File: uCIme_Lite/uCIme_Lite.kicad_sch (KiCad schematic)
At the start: 0 parts

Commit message: lite: Added power jack power control schematic.
Signed-off-by: Adrien Ricciardi <aricciardi@baylibre.com>
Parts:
- added J? (x2): JACK-C-PC-10A-RA(R), PJ-082BH:JACK-C-PC-10A-RA(R), symbol PJ-082BH:JACK-C-PC-10A-RA(R)
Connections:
- new net GND: J?.2, J?.2, J?.S1 (Shield), J?.S1 (Shield), J?.S2 (Shield), J?.S2 (Shield), J?.S3 (Shield), J?.S3 (Shield), J?.S4 (Shield), J?.S4 (Shield)
- new net Power Management/INPUT_JACK_V+: J?.1
- new net Power Management/OUTPUT_JACK_V+: J?.1
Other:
- added sheet Power Management (Power_Management.kicad_sch)
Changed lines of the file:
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@@
 (kicad_sch (version 20211123) (generator eeschema)
-  (paper "A4")
+  (paper "A3")
   (title_block
     (title "uCIme Lite main page")
@@
     (company "(C) BayLibre")
   )
+  (junction (at 132.08 57.15) (diameter 0) (color 0 0 0 0)
+  )
+  (junction (at 281.94 57.15) (diameter 0) (color 0 0 0 0)
+  )
+  (wire (pts (xy 281.94 50.8) (xy 283.21 50.8))
+    (stroke (width 0) (type default) (color 0 0 0 0))
+  )
+  (wire (pts (xy 130.81 45.72) (xy 177.8 45.72))
+    (stroke (width 0) (type default) (color 0 0 0 0))
+  )
+  (wire (pts (xy 123.19 57.15) (xy 132.08 57.15))
+    (stroke (width 0) (type default) (color 0 0 0 0))
+  )
+  (wire (pts (xy 236.22 45.72) (xy 283.21 45.72))
+    (stroke (width 0) (type default) (color 0 0 0 0))
+  )
+  (wire (pts (xy 130.81 50.8) (xy 132.08 50.8))
+    (stroke (width 0) (type default) (color 0 0 0 0))
+  )
+  (wire (pts (xy 132.08 50.8) (xy 132.08 57.15))
+    (stroke (width 0) (type default) (color 0 0 0 0))
+  )
+  (wire (pts (xy 290.83 55.88) (xy 290.83 57.15))
+    (stroke (width 0) (type default) (color 0 0 0 0))
+  )
+  (wire (pts (xy 281.94 57.15) (xy 290.83 57.15))
+    (stroke (width 0) (type default) (color 0 0 0 0))
+  )
+  (wire (pts (xy 281.94 50.8) (xy 281.94 57.15))
+    (stroke (width 0) (type default) (color 0 0 0 0))
+  )
+  (wire (pts (xy 132.08 57.15) (xy 132.08 58.42))
+    (stroke (width 0) (type default) (color 0 0 0 0))
+  )
+  (wire (pts (xy 281.94 57.15) (xy 281.94 58.42))
+    (stroke (width 0) (type default) (color 0 0 0 0))
+  )
+  (wire (pts (xy 123.19 55.88) (xy 123.19 57.15))
+    (stroke (width 0) (type default) (color 0 0 0 0))
+  )
+  (symbol (lib_id "PJ-082BH:JACK-C-PC-10A-RA(R)") (at 290.83 48.26 0) (mirror y) (unit 1)
+    (in_bom yes) (on_board yes) (fields_autoplaced)
+    (property "Reference" "J?" (id 0) (at 297.18 47.3455 0)
+      (effects (font (size 1.27 1.27)) (justify right))
+    )
+    (property "Value" "JACK-C-PC-10A-RA(R)" (id 1) (at 297.18 49.8855 0)
+      (effects (font (size 1.27 1.27)) (justify right))
+    )
+    (property "Footprint" "PJ-082BH:JACK-C-PC-10A-RA(R)" (id 2) (at 290.83 48.26 0)
+      (effects (font (size 1.27 1.27)) hide)
+    )
+    (property "Datasheet" "" (id 3) (at 290.83 48.26 0)
+      (effects (font (size 1.27 1.27)) hide)
+    )
+    (pin "1")
+    (pin "2")
+    (pin "S1")
+    (pin "S2")
+    (pin "S3")
+    (pin "S4")
+  )
+  (symbol (lib_id "PJ-082BH:JACK-C-PC-10A-RA(R)") (at 123.19 48.26 0) (unit 1)
+    (in_bom yes) (on_board yes) (fields_autoplaced)
+    (property "Reference" "J?" (id 0) (at 123.19 39.37 0))
+    (property "Value" "JACK-C-PC-10A-RA(R)" (id 1) (at 123.19 41.91 0))
+    (property "Footprint" "PJ-082BH:JACK-C-PC-10A-RA(R)" (id 2) (at 123.19 48.26 0)
+      (effects (font (size 1.27 1.27)) hide)
+    )
+    (property "Datasheet" "" (id 3) (at 123.19 48.26 0)
+      (effects (font (size 1.27 1.27)) hide)
+    )
+    (pin "1")
+    (pin "2")
+    (pin "S1")
+    (pin "S2")
+    (pin "S3")
+    (pin "S4")
+  )
+  (symbol (lib_id "power:GND") (at 281.94 58.42 0) (unit 1)
+    (in_bom yes) (on_board yes) (fields_autoplaced)
+    (property "Reference" "#PWR?" (id 0) (at 281.94 64.77 0)
+      (effects (font (size 1.27 1.27)) hide)
+    )
+    (property "Value" "GND" (id 1) (at 281.94 63.5 0))
+    (property "Footprint" "" (id 2) (at 281.94 58.42 0)
+      (effects (font (size 1.27 1.27)) hide)
+    )
+    (property "Datasheet" "" (id 3) (at 281.94 58.42 0)
+      (effects (font (size 1.27 1.27)) hide)
+    )
+    (pin "1")
+  )
+  (symbol (lib_id "power:GND") (at 132.08 58.42 0) (unit 1)
+    (in_bom yes) (on_board yes) (fields_autoplaced)
+    (property "Reference" "#PWR?" (id 0) (at 132.08 64.77 0)
+      (effects (font (size 1.27 1.27)) hide)
+    )
+    (property "Value" "GND" (id 1) (at 132.08 63.5 0))
+    (property "Footprint" "" (id 2) (at 132.08 58.42 0)
+      (effects (font (size 1.27 1.27)) hide)
+    )
+    (property "Datasheet" "" (id 3) (at 132.08 58.42 0)
+      (effects (font (size 1.27 1.27)) hide)
+    )
+    (pin "1")
+  )
+  (sheet (at 177.8 39.37) (size 58.42 31.75) (fields_autoplaced)
+    (stroke (width 0.1524) (type solid) (color 0 0 0 0))
+    (fill (color 0 0 0 0.0000))
+    (property "Sheet name" "Power Management" (id 0) (at 177.8 38.6584 0)
+      (effects (font (size 1.27 1.27)) (justify left bottom))
+    )
+    (property "Sheet file" "Power_Management.kicad_sch" (id 1) (at 177.8 71.7046 0)
+      (effects (font (size 1.27 1.27)) (justify left top))
+    )
+    (pin "INPUT_JACK_V+" input (at 177.8 45.72 180)
+      (effects (font (size 1.27 1.27)) (justify left))
+    )
+    (pin "OUTPUT_JACK_V+" output (at 236.22 45.72 0)
+      (effects (font (size 1.27 1.27)) (justify right))
+    )
+    (pin "JACK_ENABLE" input (at 220.98 71.12 270)
+      (effects (font (size 1.27 1.27)) (justify left))
+    )
+  )
   (sheet_instances
     (path "/" (page "1"))
+    (path "/b72074d7-db6e-4ce2-896d-216adccf1d19" (page "2"))
+  )
+  (symbol_instances
+    (path "/b72074d7-db6e-4ce2-896d-216adccf1d19/02fafa4a-7b73-4e81-8da5-132c6b5c9bff"
+      (reference "#PWR?") (unit 1) (value "GND") (footprint "")
+    )
+    (path "/b72074d7-db6e-4ce2-896d-216adccf1d19/35a86e98-46cc-46df-ad53-81efd104ac95"
+      (reference "#PWR?") (unit 1) (value "GND") (footprint "")
+    )
+    (path "/b72074d7-db6e-4ce2-896d-216adccf1d19/635934cd-3f03-40e6-aa6f-441bbb697ee2"
+      (reference "#PWR?") (unit 1) (value "GND") (footprint "")
+    )
+    (path "/b72074d7-db6e-4ce2-896d-216adccf1d19/7c913419-8c7e-474a-a151-4292df2a9063"
+      (reference "#PWR?") (unit 1) (value "GND") (footprint "")
+    )
+    (path "/b72074d7-db6e-4ce2-896d-216adccf1d19/82d1e808-369e-4a11-819a-83d565227eb4"
+      (reference "#PWR?") (unit 1) (value "GND") (footprint "")
+    )
+    (path "/b72074d7-db6e-4ce2-896d-216adccf1d19/98f27e05-bd7c-4098-9b75-20ce5d30fae5"
+      (reference "#PWR?") (unit 1) (value "GND") (footprint "")
+    )
+    (path "/aaee36d0-4dcf-457a-8eaa-8cb8fea45041"
+      (reference "#PWR?") (unit 1) (value "GND") (footprint "")
+    )
+    (path "/de94efd2-e5d2-4545-9075-dd7613e5777f"
+      (reference "#PWR?") (unit 1) (value "GND") (footprint "")
+    )
+    (path "/b72074d7-db6e-4ce2-896d-216adccf1d19/e31b32d0-c0c6-443a-8ef3-a94aeee3b208"
+      (reference "#PWR?") (unit 1) (value "GND") (footprint "")
+    )
+    (path "/b72074d7-db6e-4ce2-896d-216adccf1d19/17bc7eea-81f3-448e-95b1-8b446b2817f2"
+      (reference "C?") (unit 1) (value "220n") (footprint "Capacitor_SMD:C_0805_2012Metric")
+    )
+    (path "/b72074d7-db6e-4ce2-896d-216adccf1d19/465ff876-8b5f-4366-b4a3-31a49fbb8eed"
+      (reference "C?") (unit 1) (value "220n") (footprint "Capacitor_SMD:C_0805_2012Metric")
+    )
+    (path "/b72074d7-db6e-4ce2-896d-216adccf1d19/630f389e-df29-4fb4-a243-3d74878f7967"
+      (reference "C?") (unit 1) (value "100n") (footprint "Capacitor_SMD:C_0805_2012Metric")
+    )
+    (path "/b72074d7-db6e-4ce2-896d-216adccf1d19/a145c277-00e6-476a-b587-453aa354ab19"
+      (reference "C?") (unit 1) (value "100n") (footprint "Capacitor_SMD:C_0805_2012Metric")
+    )
+    (path "/03e02d60-ba51-4f77-a312-8d67a4adcc67"
+      (reference "J?") (unit 1) (value "JACK-C-PC-10A-RA(R)") (footprint "PJ-082BH:JACK-C-PC-10A-RA(R)")
+    )
+    (path "/3071b057-73f1-47ad-9445-a53f1a251bbe"
+      (reference "J?") (unit 1) (value "JACK-C-PC-10A-RA(R)") (footprint "PJ-082BH:JACK-C-PC-10A-RA(R)")
+    )
+    (path "/b72074d7-db6e-4ce2-896d-216adccf1d19/24df8571-9618-4f38-9191-19c2d92e80ea"
+      (reference "Q?") (unit 1) (value "BUK7M27-80EX") (footprint "Package_TO_SOT_SMD:LFPAK33")
+    )
+    (path "/b72074d7-db6e-4ce2-896d-216adccf1d19/bae3b56c-6075-495b-ac2a-b15d5aaa6fb6"
+      (reference "Q?") (unit 1) (value "BUK7M27-80EX") (footprint "Package_TO_SOT_SMD:LFPAK33")
+    )
+    (path "/b72074d7-db6e-4ce2-896d-216adccf1d19/21cf5ff6-9362-4b6b-a0e8-4d769b623a57"
+      (reference "R?") (unit 1) (value "2.4K") (footprint "Resistor_SMD:R_0805_2012Metric")
+    )
+    (path "/b72074d7-db6e-4ce2-896d-216adccf1d19/8e4f213e-c272-4cc1-a885-011733cd1c99"
+      (reference "R?") (unit 1) (value "10K") (footprint "Resistor_SMD:R_0603_1608Metric")
+    )
+    (path "/b72074d7-db6e-4ce2-896d-216adccf1d19/b2b14a25-12a4-4a13-acce-e2b1fa675d65"
+      (reference "R?") (unit 1) (value "2.4K") (footprint "Resistor_SMD:R_0805_2012Metric")
+    )
+    (path "/b72074d7-db6e-4ce2-896d-216adccf1d19/b41c0c4f-3eb3-4292-98d3-8d6b3c2fdb3e"
+      (reference "R?") (unit 1) (value "100K") (footprint "Resistor_SMD:R_0805_2012Metric")
+    )
+    (path "/b72074d7-db6e-4ce2-896d-216adccf1d19/b6fd1149-5a54-4cd5-b461-db5cd51b274d"
+      (reference "R?") (unit 1) (value "100K") (footprint "Resistor_SMD:R_0805_2012Metric")
+    )
+    (path "/b72074d7-db6e-4ce2-896d-216adccf1d19/661111ac-6796-49e3-97a6-9e38a52c1059"
+      (reference "U?") (unit 1) (value "LM74502") (footprint "Package_TO_SOT_SMD:SOT-23-8")
+    )
+    (path "/b72074d7-db6e-4ce2-896d-216adccf1d19/8e393669-7079-4850-859c-bf3b4331f2b2"
+      (reference "U?") (unit 1) (value "LM74502") (footprint "Package_TO_SOT_SMD:SOT-23-8")
+    )
   )
 )

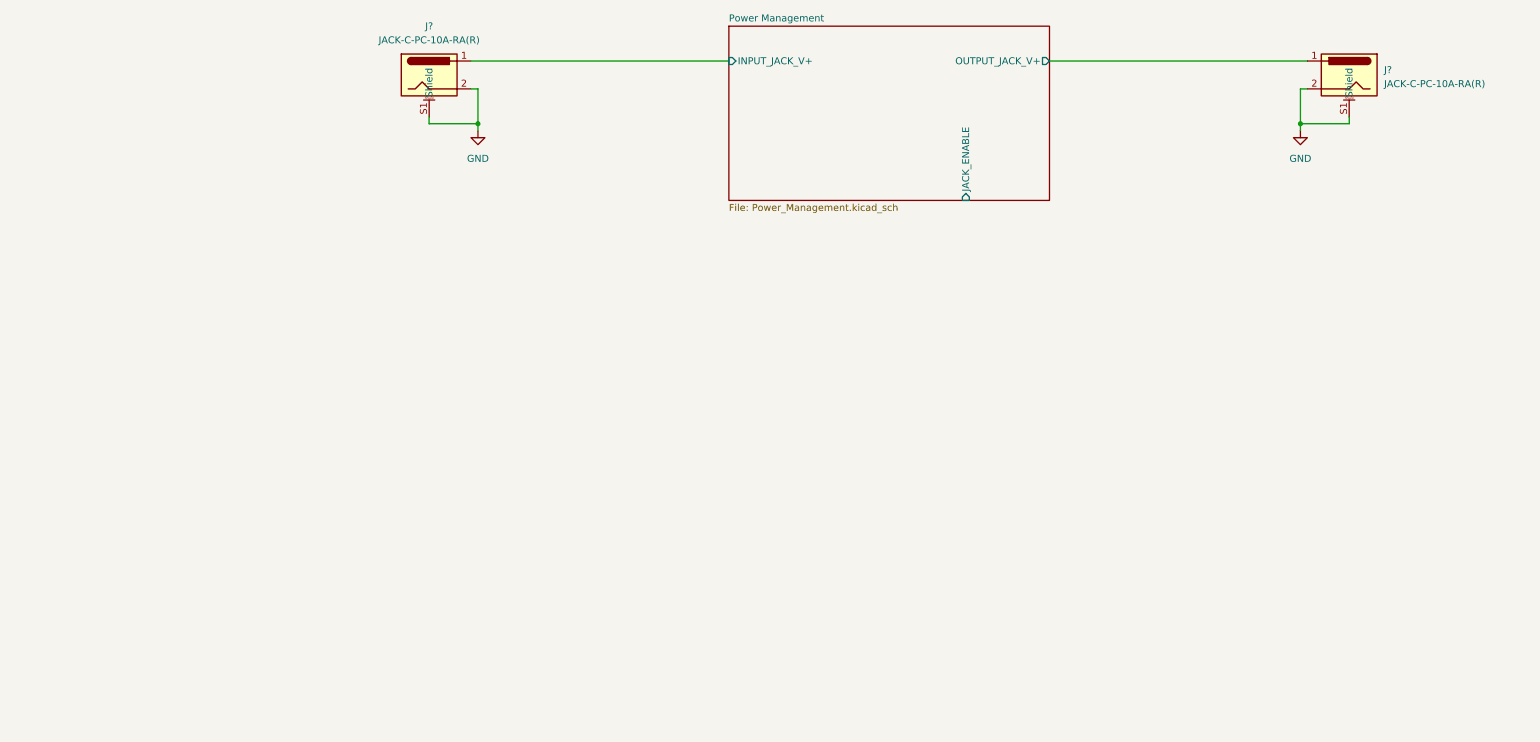
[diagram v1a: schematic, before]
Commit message: lite: Added USB-C connectors power control and data passthrough.
Signed-off-by: Adrien Ricciardi <aricciardi@baylibre.com>
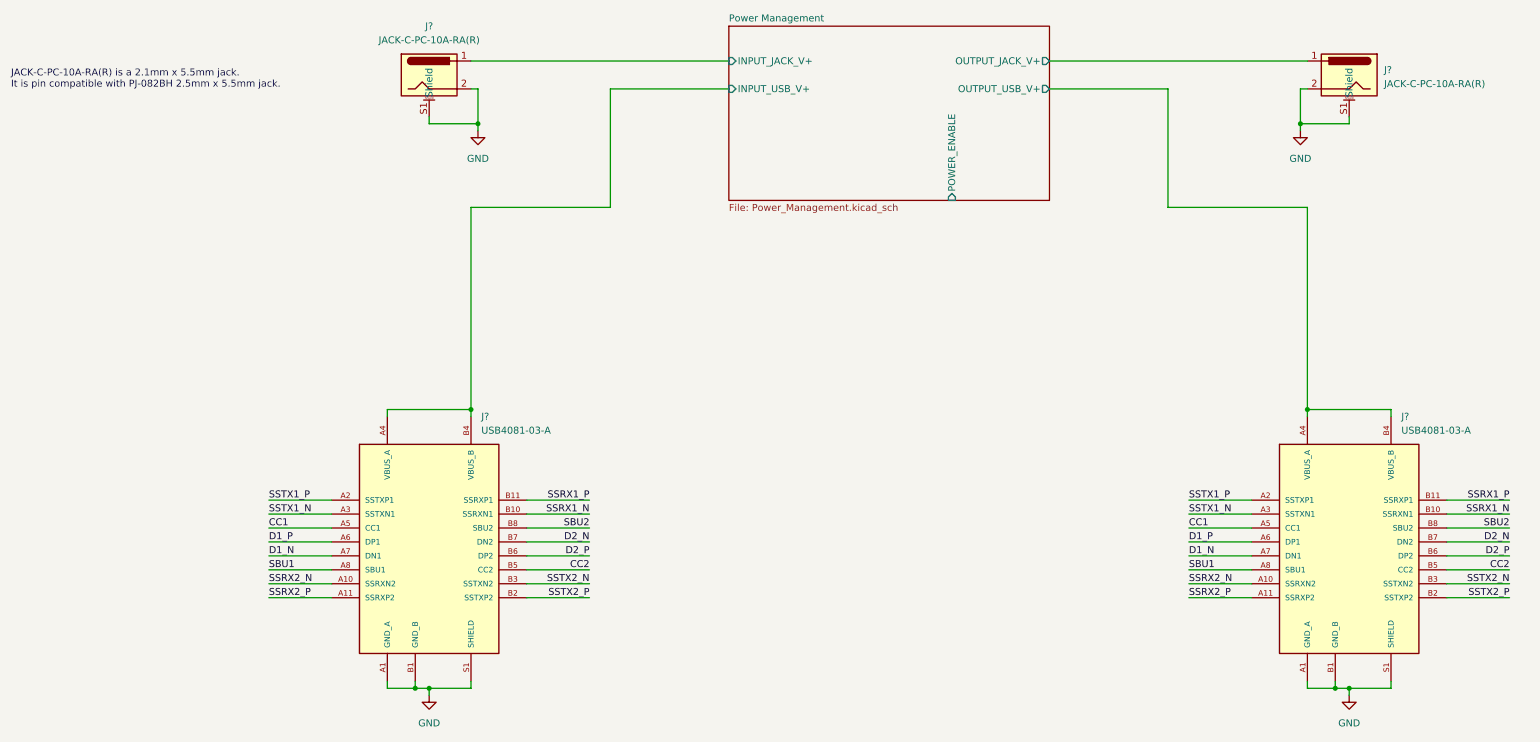
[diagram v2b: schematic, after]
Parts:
- added J? (x2): USB4081-03-A, USB4081:USB4081-03-A, symbol USB4081:USB4081-03-A
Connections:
- net GND: now also J?.A1 (GND_A), J?.A1 (GND_A), J?.A12 (GND_A), J?.A12 (GND_A), J?.B1 (GND_B), J?.B1 (GND_B), J?.B12 (GND_B), J?.B12 (GND_B), J?.S1 (SHIELD), J?.S1 (SHIELD), J?.S2 (SHIELD), J?.S2 (SHIELD), J?.S3 (SHIELD), J?.S3 (SHIELD), J?.S4 (SHIELD), J?.S4 (SHIELD), J?.S5 (SHIELD), J?.S5 (SHIELD), J?.S6 (SHIELD), J?.S6 (SHIELD)
- new net CC1: J?.A5 (CC1), J?.A5 (CC1)
- new net CC2: J?.B5 (CC2), J?.B5 (CC2)
- new net D1_N: J?.A7 (DN1), J?.A7 (DN1)
- new net D1_P: J?.A6 (DP1), J?.A6 (DP1)
- new net D2_N: J?.B7 (DN2), J?.B7 (DN2)
- new net D2_P: J?.B6 (DP2), J?.B6 (DP2)
- new net SBU1: J?.A8 (SBU1), J?.A8 (SBU1)
- new net SBU2: J?.B8 (SBU2), J?.B8 (SBU2)
- new net SSRX1_N: J?.B10 (SSRXN1), J?.B10 (SSRXN1)
- new net SSRX1_P: J?.B11 (SSRXP1), J?.B11 (SSRXP1)
- new net SSRX2_N: J?.A10 (SSRXN2), J?.A10 (SSRXN2)
- new net SSRX2_P: J?.A11 (SSRXP2), J?.A11 (SSRXP2)
- new net SSTX1_N: J?.A3 (SSTXN1), J?.A3 (SSTXN1)
- new net SSTX1_P: J?.A2 (SSTXP1), J?.A2 (SSTXP1)
- new net SSTX2_N: J?.B3 (SSTXN2), J?.B3 (SSTXN2)
- new net SSTX2_P: J?.B2 (SSTXP2), J?.B2 (SSTXP2)
- new net VBUS_A: J?.A4 (VBUS_A), J?.A4 (VBUS_A), J?.A9 (VBUS_A), J?.A9 (VBUS_A), J?.B4 (VBUS_B), J?.B4 (VBUS_B), J?.B9 (VBUS_B), J?.B9 (VBUS_B)
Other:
- sheet Power Management ports: added INPUT_USB_V+, OUTPUT_USB_V+, POWER_ENABLE; removed JACK_ENABLE
- note added: "JACK-C-PC-10A-RA(R) is a 2.1mm x 5.5mm jack. It is pin compatible with PJ-082BH 2.5mm x 5.5mm jack."
